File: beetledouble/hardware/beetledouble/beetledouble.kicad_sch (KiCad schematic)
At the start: 26 parts, among them J1 XT30PW-M, J2 rxin, J6 prog connector, U1 78L12G-AB3-R, U2 DD4012SB, U3 ATtiny1614-SS

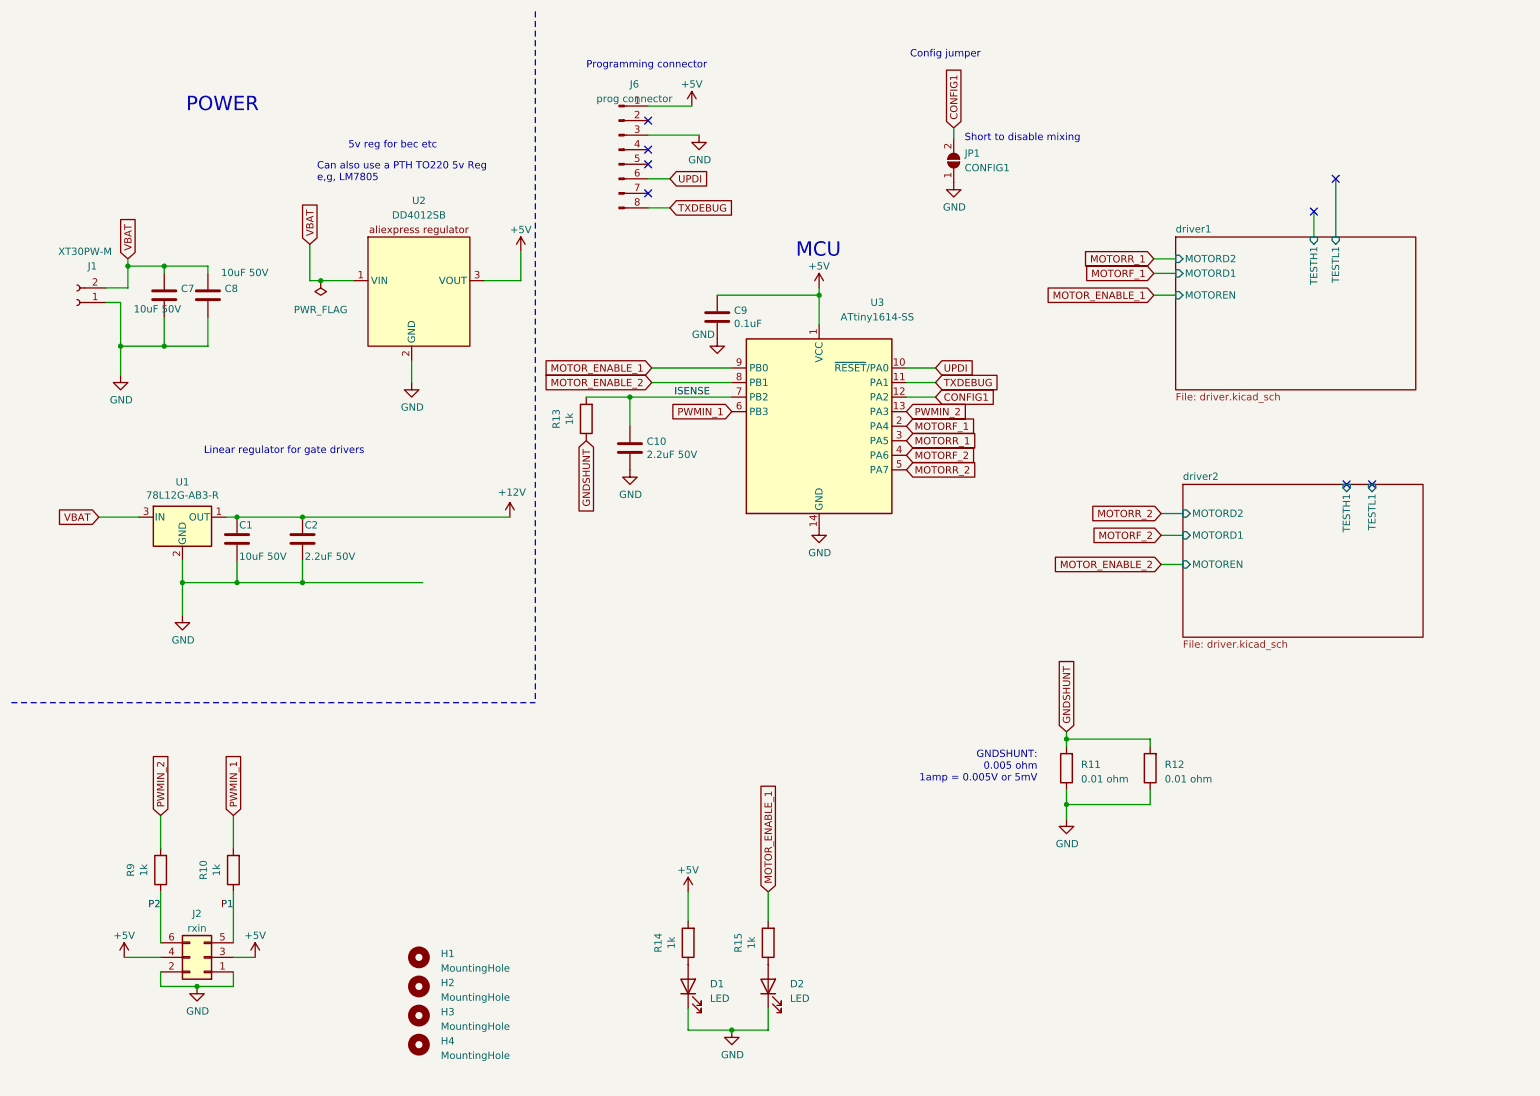
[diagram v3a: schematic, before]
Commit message: Pin updates to get ADC pins and VSENSE and ISENSE etc
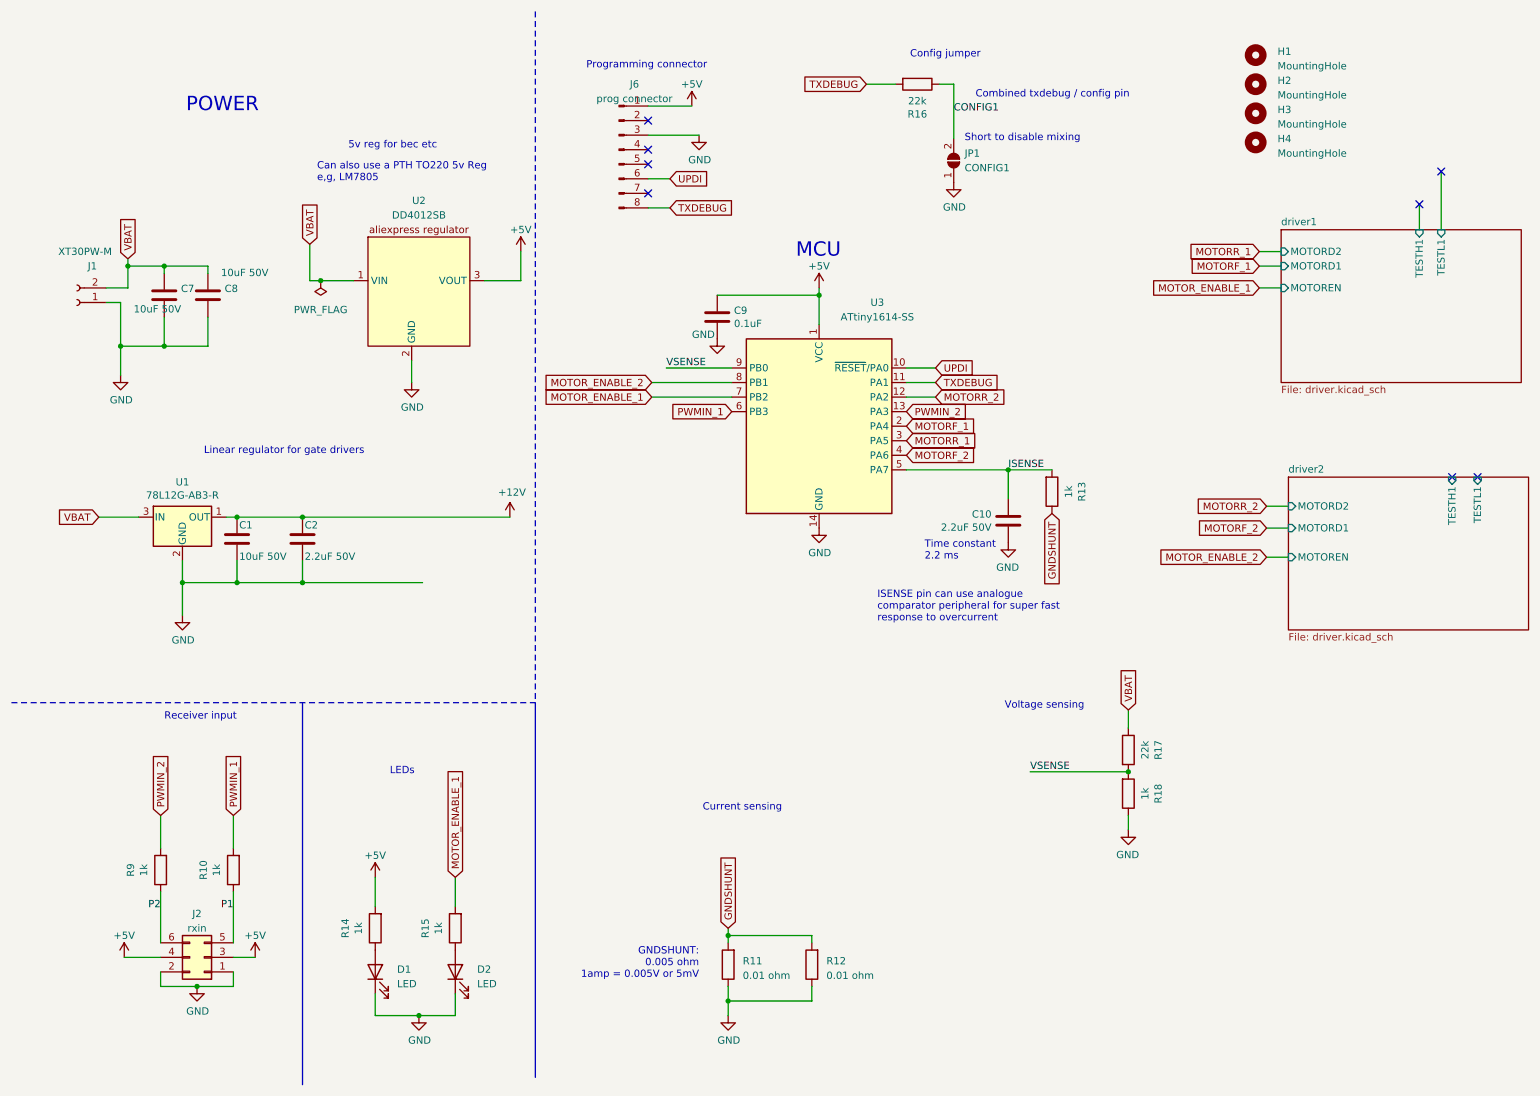
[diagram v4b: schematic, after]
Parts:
- added R16, R17: 22k, Resistor_SMD:R_0603_1608Metric, symbol Device:R
- added R18: 1k, Resistor_SMD:R_0603_1608Metric, symbol Device:R
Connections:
- net CONFIG1: now also R16.1; no longer U3.12 (PA2)
- net GND: now also R18.1
- net ISENSE: now also U3.5 (PA7); no longer U3.7 (PB2)
- net MOTORR_2: now also U3.12 (PA2); no longer U3.5 (PA7)
- net MOTOR_ENABLE_1: now also U3.7 (PB2); no longer U3.9 (PB0)
- net TXDEBUG: now also R16.2
- net VBAT: now also R17.1
- new net VSENSE: R17.2, R18.2, U3.9 (PB0)
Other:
- note added: "Combined txdebug / config pin"
- note added: "Current sensing"
- note added: "ISENSE pin can use analogue comparator peripheral for super fast response to overcurrent"
- note added: "LEDs"
- note added: "Receiver input"
- note added: "Time constant 2.2 ms"
- note added: "Voltage sensing"
- moved on the sheet: C10, D1, D2, H1, H2, H3, H4, R11, R12, R13, R14, R15

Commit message: lcsc ids and comments and stuff
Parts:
- R16, R17: LCSC (none) -> C31850
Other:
- note added: "Can use analogue sensing to read this pin at bootup"
- note added: "GPIO internal pullup nominal 35k ohm"
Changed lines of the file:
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@@
+    (effects (font (size 1.27 1.27)) (justify left bottom))
+  )
+  (text "Config jumper" (at 149.86 15.24 0)
+    (effects (font (size 1.27 1.27)) (justify left bottom))
+  )
+  (text "GPIO internal pullup nominal 35k ohm" (at 149.86 18.415 0)
+    (effects (font (size 1.27 1.27)) (justify left bottom))
+  )
+  (text "Can use analogue sensing to read this pin at bootup"
+    (at 149.86 21.59 0)
     (effects (font (size 1.27 1.27)) (justify left bottom))
   )
@@
   (text "ISENSE pin can use analogue \ncomparator peripheral for super fast\nresponse to overcurrent"
     (at 162.56 118.11 0)
-    (effects (font (size 1.27 1.27)) (justify left bottom))
-  )
-  (text "Config jumper" (at 168.275 19.685 0)
     (effects (font (size 1.27 1.27)) (justify left bottom))
   )
@@
       (effects (font (size 1.27 1.27)) hide)
     )
-    (property "LCSC" "" (id 4) (at 169.545 24.13 0)
+    (property "LCSC" "C31850" (id 4) (at 169.545 24.13 0)
       (effects (font (size 1.27 1.27)) hide)
     )
@@
       (effects (font (size 1.27 1.27)) hide)
     )
-    (property "LCSC" "" (id 4) (at 206.375 140.335 0)
-      (effects (font (size 1.27 1.27)) hide)
-    )
+    (property "LCSC" "C31850" (id 4) (at 206.375 140.335 0)
+      (effects (font (size 1.27 1.27)) hide)
+    )

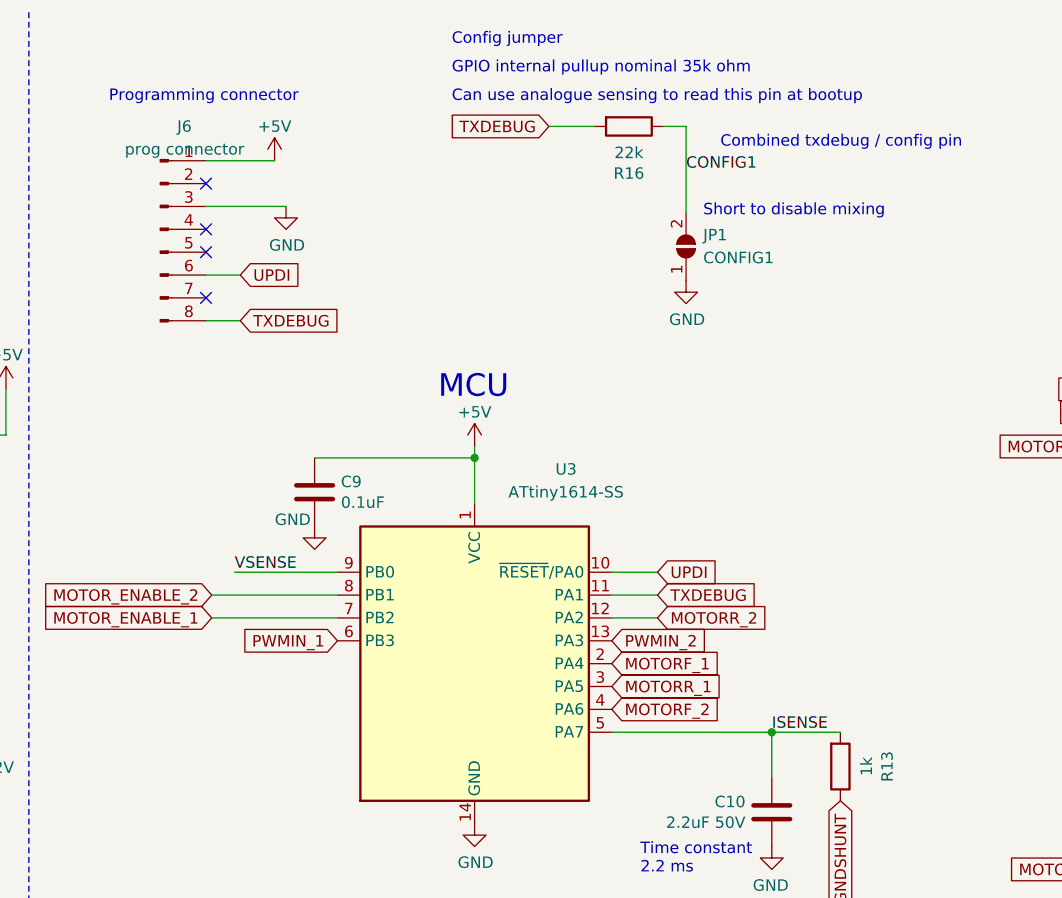
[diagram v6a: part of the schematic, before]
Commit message: Resistor to smooth out mcu power slightly
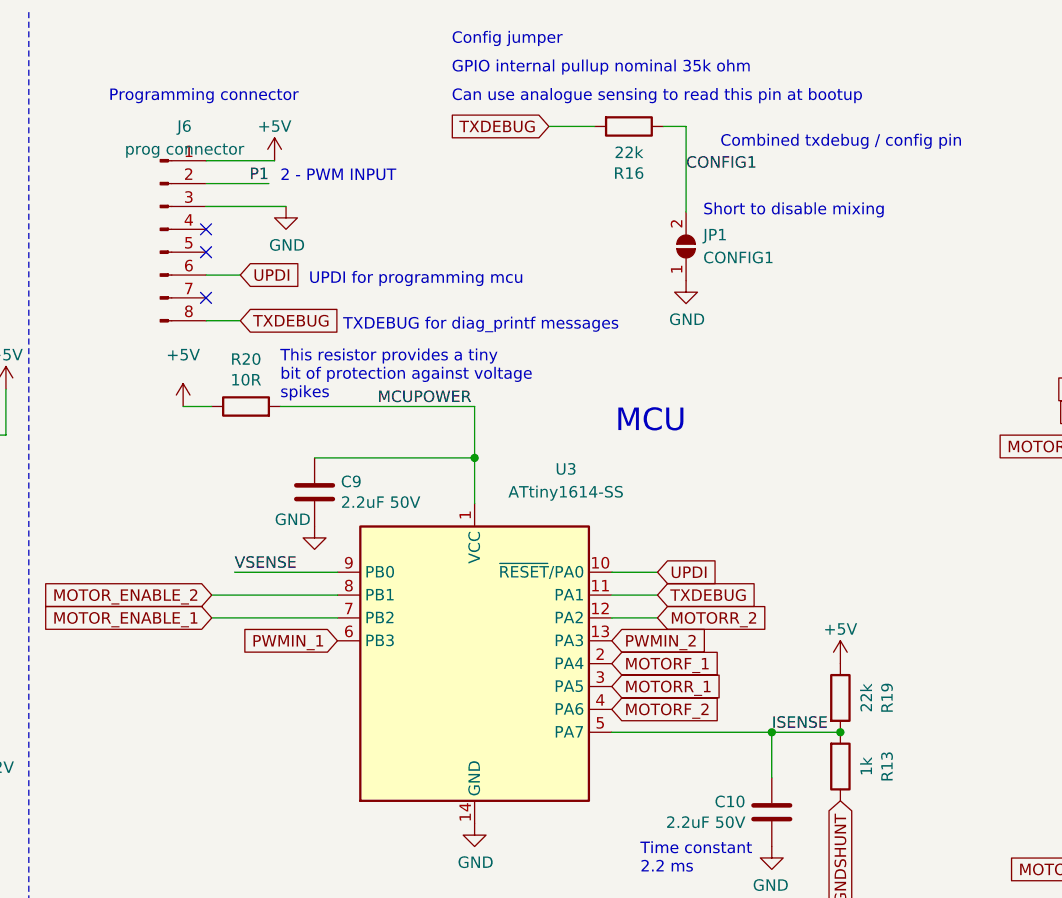
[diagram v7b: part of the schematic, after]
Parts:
- added R19: 22k, Resistor_SMD:R_0603_1608Metric, symbol Device:R
- added R20: 10R, Resistor_SMD:R_0603_1608Metric, symbol Device:R
- C9: value 0.1uF -> 2.2uF 50V; LCSC C14663 -> C162273
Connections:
- net +5V: now also R19.1, R20.1; no longer C9.1, U3.1 (VCC)
- net ISENSE: now also R19.2
- net P1: now also J6.2 (Pin_2)
- new net MCUPOWER: C9.1, R20.2, U3.1 (VCC)
- no-connect marks 8 -> 7
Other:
- note added: "2 - PWM INPUT"
- note added: "TXDEBUG for diag_printf messages"
- note added: "This resistor provides a tiny bit of protection against voltage spikes"
- note added: "UPDI for programming mcu"
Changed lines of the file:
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@@
   (junction (at 152.4 60.96) (diameter 0.9144) (color 0 0 0 0))
   (junction (at 185.42 91.44) (diameter 0) (color 0 0 0 0))
+  (junction (at 193.04 91.44) (diameter 0) (color 0 0 0 0))
   (junction (at 206.375 144.145) (diameter 0) (color 0 0 0 0))
-  (no_connect (at 122.555 30.48))
   (no_connect (at 122.555 35.56))
   (no_connect (at 122.555 38.1))
@@
     (stroke (width 0) (type solid) (color 0 0 0 0))
   )
+  (wire (pts (xy 120.015 55.245) (xy 123.19 55.245))
+    (stroke (width 0) (type default) (color 0 0 0 0))
+  )
   (wire (pts (xy 122.555 27.94) (xy 130.175 27.94))
     (stroke (width 0) (type solid) (color 0 0 0 0))
+  )
+  (wire (pts (xy 122.555 30.48) (xy 129.54 30.48))
+    (stroke (width 0) (type default) (color 0 0 0 0))
   )
   (wire (pts (xy 122.555 33.02) (xy 131.445 33.02))
@@
     (stroke (width 0) (type solid) (color 0 0 0 0))
   )
-  (wire (pts (xy 152.4 59.69) (xy 152.4 60.96))
+  (wire (pts (xy 152.4 55.245) (xy 130.81 55.245))
+    (stroke (width 0) (type default) (color 0 0 0 0))
+  )
+  (wire (pts (xy 152.4 55.245) (xy 152.4 60.96))
     (stroke (width 0) (type solid) (color 0 0 0 0))
   )
@@
     (effects (font (size 1.27 1.27)) (justify left bottom))
   )
+  (text "2 - PWM INPUT" (at 130.81 30.48 0)
+    (effects (font (size 1.27 1.27)) (justify left bottom))
+  )
+  (text "This resistor provides a tiny\nbit of protection against voltage\nspikes"
+    (at 130.81 54.61 0)
+    (effects (font (size 1.27 1.27)) (justify left bottom))
+  )
   (text "GNDSHUNT:\n0.005 ohm\n1amp = 0.005V or 5mV" (at 131.445 180.34 180)
     (effects (font (size 1.27 1.27)) (justify right bottom))
@@
     (effects (font (size 1.27 1.27)) (justify left bottom))
   )
+  (text "UPDI for programming mcu" (at 133.985 41.91 0)
+    (effects (font (size 1.27 1.27)) (justify left bottom))
+  )
+  (text "TXDEBUG for diag_printf messages" (at 137.795 46.99 0)
+    (effects (font (size 1.27 1.27)) (justify left bottom))
+  )
   (text "Config jumper" (at 149.86 15.24 0)
     (effects (font (size 1.27 1.27)) (justify left bottom))
@@
     (effects (font (size 1.27 1.27)) (justify left bottom))
   )
-  (text "MCU" (at 156.21 54.61 180)
-    (effects (font (size 2.5 2.5)) (justify right bottom))
-  )
   (text "ISENSE pin can use analogue \ncomparator peripheral for super fast\nresponse to overcurrent"
     (at 162.56 118.11 0)
@@
     (effects (font (size 1.27 1.27)) (justify left bottom))
   )
+  (text "MCU" (at 175.895 58.42 180)
+    (effects (font (size 2.5 2.5)) (justify right bottom))
+  )
   (text "Short to disable mixing" (at 177.8 34.29 0)
     (effects (font (size 1.27 1.27)) (justify left bottom))
@@
   )
   (label "VSENSE" (at 125.73 73.66 0)
+    (effects (font (size 1.27 1.27)) (justify left bottom))
+  )
+  (label "P1" (at 129.54 30.48 180)
+    (effects (font (size 1.27 1.27)) (justify right bottom))
+  )
+  (label "MCUPOWER" (at 141.605 55.245 0)
     (effects (font (size 1.27 1.27)) (justify left bottom))
   )
@@
     (pin "1")
   )
+  (symbol (lib_id "power:+5V") (at 120.015 55.245 0) (unit 1)
+    (in_bom yes) (on_board yes) (fields_autoplaced)
+    (property "Reference" "#PWR016" (id 0) (at 120.015 59.055 0)
+      (effects (font (size 1.27 1.27)) hide)
+    )
+    (property "Value" "+5V" (id 1) (at 120.015 49.53 0))
+    (property "Footprint" "" (id 2) (at 120.015 55.245 0)
+      (effects (font (size 1.27 1.27)) hide)
+    )
+    (property "Datasheet" "" (id 3) (at 120.015 55.245 0)
+      (effects (font (size 1.27 1.27)) hide)
+    )
+    (pin "1")
+  )
   (symbol (lib_id "power:+5V") (at 130.175 27.94 0) (unit 1)
     (in_bom yes) (on_board yes) (fields_autoplaced)
@@
     (pin "1")
   )
-  (symbol (lib_id "power:+5V") (at 152.4 59.69 0) (unit 1)
-    (in_bom yes) (on_board yes) (fields_autoplaced)
-    (property "Reference" "#PWR016" (id 0) (at 152.4 63.5 0)
-      (effects (font (size 1.27 1.27)) hide)
-    )
-    (property "Value" "+5V" (id 1) (at 152.4 55.88 0))
-    (property "Footprint" "" (id 2) (at 152.4 59.69 0)
-      (effects (font (size 1.27 1.27)) hide)
-    )
-    (property "Datasheet" "" (id 3) (at 152.4 59.69 0)
+  (symbol (lib_id "power:+5V") (at 193.04 83.82 0) (unit 1)
+    (in_bom yes) (on_board yes) (fields_autoplaced)
+    (property "Reference" "#PWR024" (id 0) (at 193.04 87.63 0)
+      (effects (font (size 1.27 1.27)) hide)
+    )
+    (property "Value" "+5V" (id 1) (at 193.04 80.01 0))
+    (property "Footprint" "" (id 2) (at 193.04 83.82 0)
+      (effects (font (size 1.27 1.27)) hide)
+    )
+    (property "Datasheet" "" (id 3) (at 193.04 83.82 0)
       (effects (font (size 1.27 1.27)) hide)
     )
@@
     (pin "2")
   )
+  (symbol (lib_id "Device:R") (at 127 55.245 90) (unit 1)
+    (in_bom yes) (on_board yes)
+    (property "Reference" "R20" (id 0) (at 127 50.0188 90))
+    (property "Value" "10R" (id 1) (at 127 52.3175 90))
+    (property "Footprint" "Resistor_SMD:R_0603_1608Metric" (id 2) (at 127 57.023 90)
+      (effects (font (size 1.27 1.27)) hide)
+    )
+    (property "Datasheet" "~" (id 3) (at 127 55.245 0)
+      (effects (font (size 1.27 1.27)) hide)
+    )
+    (property "LCSC" "C22859" (id 4) (at 127 55.245 0)
+      (effects (font (size 1.27 1.27)) hide)
+    )
+    (pin "1")
+    (pin "2")
+  )
   (symbol (lib_id "Device:R") (at 136.525 177.8 180) (unit 1)
     (in_bom yes) (on_board yes) (fields_autoplaced)
@@
     (pin "2")
   )
+  (symbol (lib_id "Device:R") (at 193.04 87.63 0) (unit 1)
+    (in_bom yes) (on_board yes)
+    (property "Reference" "R19" (id 0) (at 198.2662 87.63 90))
+    (property "Value" "22k" (id 1) (at 195.9675 87.63 90))
+    (property "Footprint" "Resistor_SMD:R_0603_1608Metric" (id 2) (at 191.262 87.63 90)
+      (effects (font (size 1.27 1.27)) hide)
+    )
+    (property "Datasheet" "~" (id 3) (at 193.04 87.63 0)
+      (effects (font (size 1.27 1.27)) hide)
+    )
+    (property "LCSC" "C31850" (id 4) (at 193.04 87.63 0)
+      (effects (font (size 1.27 1.27)) hide)
+    )
+    (pin "1")
+    (pin "2")
+  )
   (symbol (lib_id "Device:R") (at 193.04 95.25 0) (mirror x) (unit 1)
     (in_bom yes) (on_board yes)
@@
       (effects (font (size 1.27 1.27)) (justify left))
     )
-    (property "Value" "0.1uF" (id 1) (at 137.5411 65.9193 0)
+    (property "Value" "2.2uF 50V" (id 1) (at 137.5411 65.9193 0)
       (effects (font (size 1.27 1.27)) (justify left))
     )
@@
       (effects (font (size 1.27 1.27)) hide)
     )
-    (property "LCSC" "C14663" (id 4) (at 134.62 64.77 0)
+    (property "LCSC" "C162273" (id 4) (at 134.62 64.77 0)
       (effects (font (size 1.27 1.27)) hide)
     )
@@
       (reference "#PWR023") (unit 1) (value "GND") (footprint "")
     )
+    (path "/c572d987-9137-447c-a778-9cd6f8acba6a"
+      (reference "#PWR024") (unit 1) (value "+5V") (footprint "")
+    )
     (path "/5120773c-2e98-4937-a9a8-d32ce1f0f467"
       (reference "#PWR0101") (unit 1) (value "GND") (footprint "")
@@
     )
     (path "/b5359845-ee9f-4a8c-86ac-cd9841c12595"
-      (reference "C9") (unit 1) (value "0.1uF") (footprint "Capacitor_SMD:C_0603_1608Metric")
+      (reference "C9") (unit 1) (value "2.2uF 50V") (footprint "Capacitor_SMD:C_0603_1608Metric")
     )
     (path "/ec931dfe-fcd6-43aa-a942-f11aa5bf6441"
@@
       (reference "R18") (unit 1) (value "1k") (footprint "Resistor_SMD:R_0603_1608Metric")
     )
+    (path "/260a9191-c4ba-4390-8b3d-0e606422240b"
+      (reference "R19") (unit 1) (value "22k") (footprint "Resistor_SMD:R_0603_1608Metric")
+    )
+    (path "/48b0075a-ad8f-43b9-8991-293b45d8b2f5"
+      (reference "R20") (unit 1) (value "10R") (footprint "Resistor_SMD:R_0603_1608Metric")
+    )
     (path "/b612c31e-0d17-46e0-a098-3e7233416658"

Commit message: MCU power fixup
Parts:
- added C19: 100nF, Capacitor_SMD:C_0603_1608Metric, symbol Device:C
- added D7: 5.1V, Diode_SMD:D_SOD-523, symbol Device:D_Zener
- R20: value 10R -> 15R; LCSC C22859 -> C22810
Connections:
- net GND: now also C19.2, D7.2 (A)
- net MCUPOWER: now also C19.1, D7.1 (K)
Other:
- note added: "Clamping Zener"
- note added: "MCU power"
- note removed: "This resistor provides a tiny bit of protection against voltage spikes"
- moved on the sheet: C1, C2, C7, C8, C9, J1, U1, U2
